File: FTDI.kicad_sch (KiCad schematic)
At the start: 23 parts, among them U5 FT4232H_VQFN, Y1 Resonator_12MHz_ABM8G

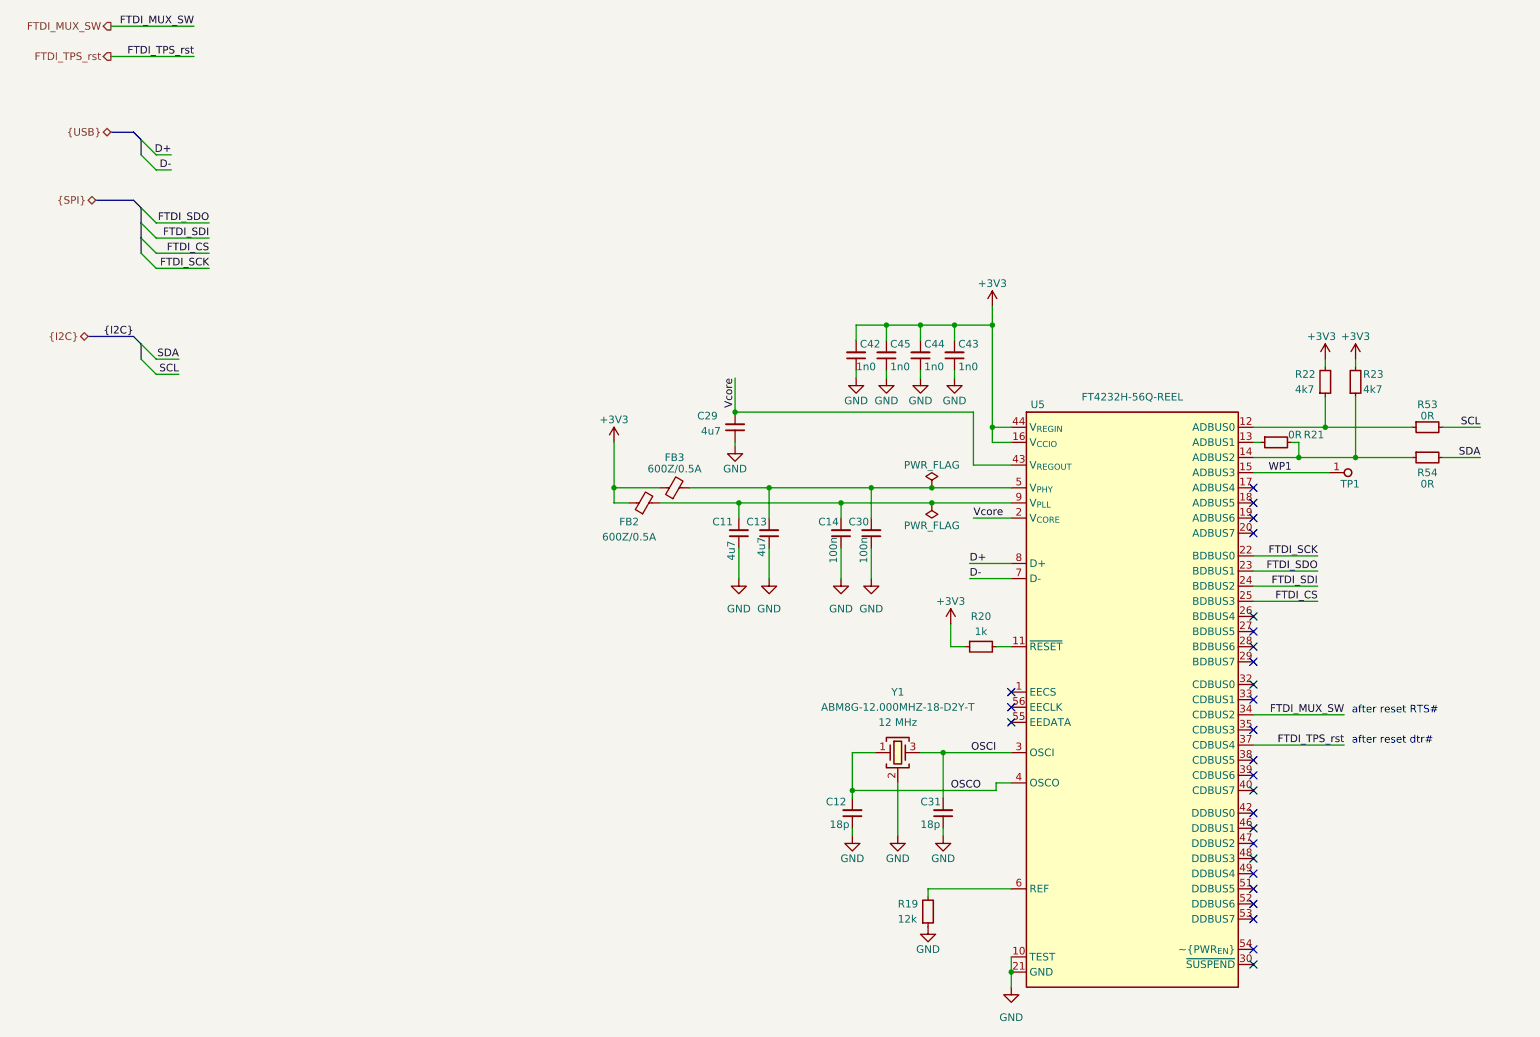
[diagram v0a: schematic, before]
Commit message: [#63274] Remove one optocoupler, add components to PCB, route PCB
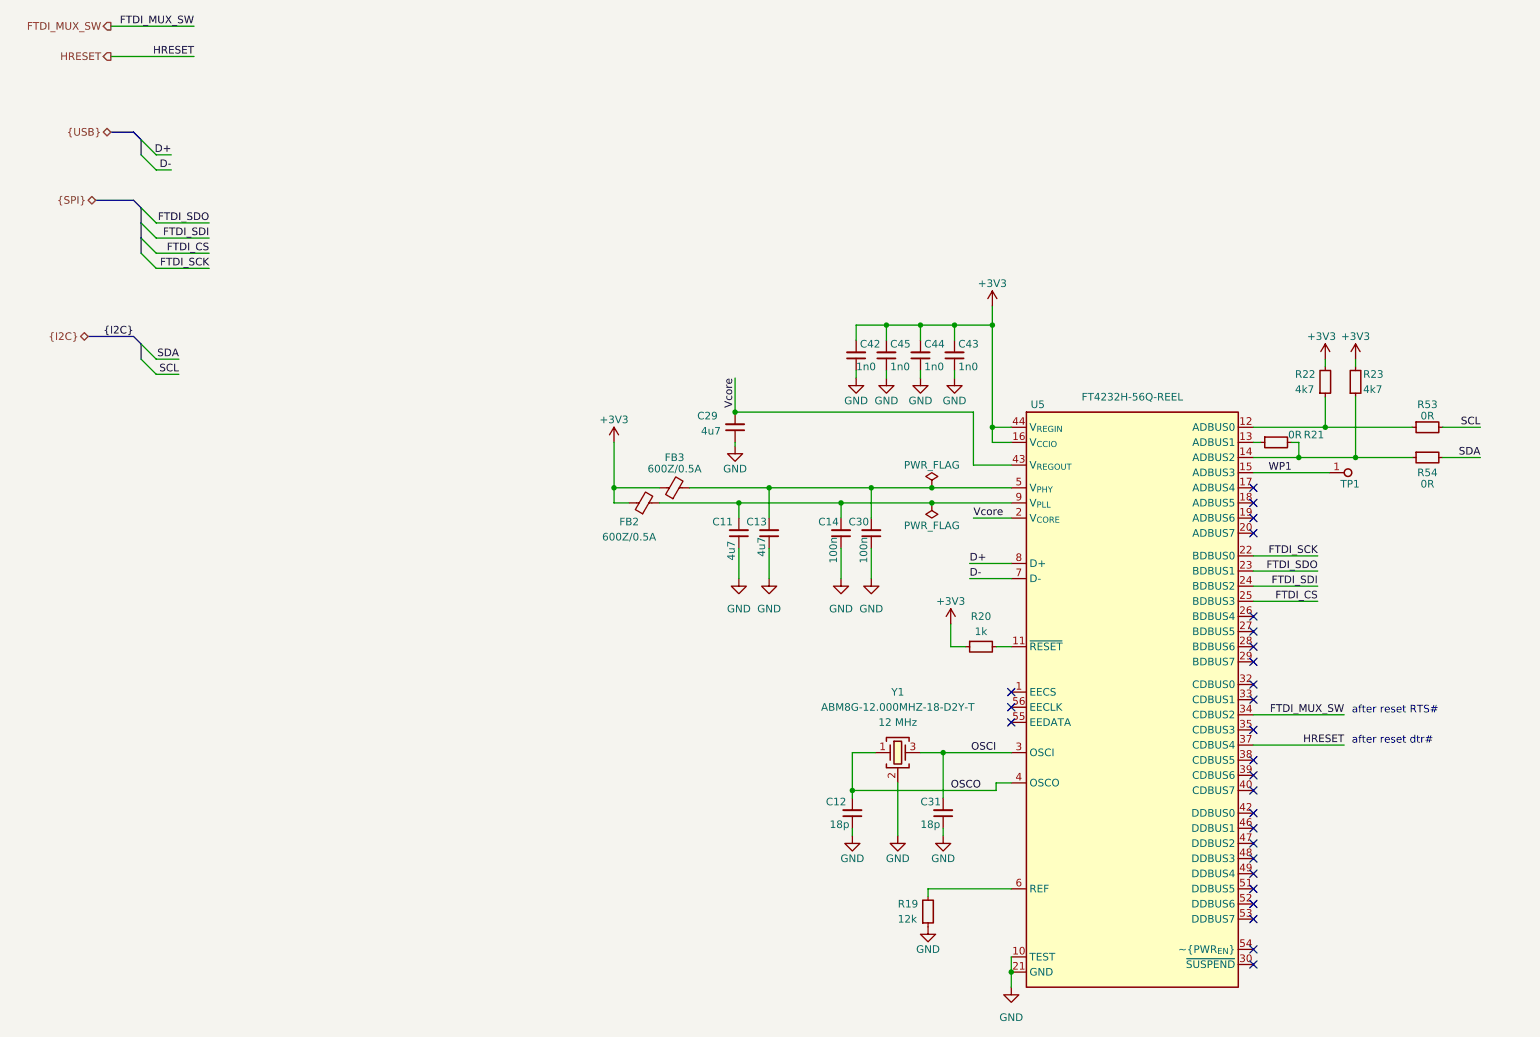
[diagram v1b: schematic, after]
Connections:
- net FTDI_TPS_rst renamed HRESET
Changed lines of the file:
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@@
     (effects (font (size 1.27 1.27)) (justify right bottom))
   )
-  (label "FTDI_TPS_rst" (at 43.18 29.21 180) (fields_autoplaced)
+  (label "HRESET" (at 43.18 29.21 180) (fields_autoplaced)
     (effects (font (size 1.27 1.27)) (justify right bottom))
   )
@@
     (effects (font (size 1.27 1.27)) (justify right bottom))
   )
-  (label "FTDI_TPS_rst" (at 236.22 144.78 180) (fields_autoplaced)
+  (label "HRESET" (at 236.22 144.78 180) (fields_autoplaced)
     (effects (font (size 1.27 1.27)) (justify right bottom))
   )
@@
     (effects (font (size 1.27 1.27)) (justify right))
   )
-  (hierarchical_label "FTDI_TPS_rst" (shape output) (at 29.21 29.21 180) (fields_autoplaced)
+  (hierarchical_label "HRESET" (shape output) (at 29.21 29.21 180) (fields_autoplaced)
     (effects (font (size 1.27 1.27)) (justify right))
   )

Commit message: [#64013] Prepare production fixes
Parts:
- TP1: footprint antmicro-footprints:TP_SMD_0.75mm -> antmicro-footprints:TP_SMD_1.5mm
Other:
- company: Antmicro ltd. -> Antmicro Ltd.
- moved on the sheet: C14, C29, C30, C42, C43, C44, C45, FB2, FB3, R22, R23
